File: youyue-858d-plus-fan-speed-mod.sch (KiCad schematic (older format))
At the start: 18 parts, among them P1 CONN_01X01, P2 CONN_01X01, P3 CONN_01X01, P4 CONN_01X01, U1 LM2904

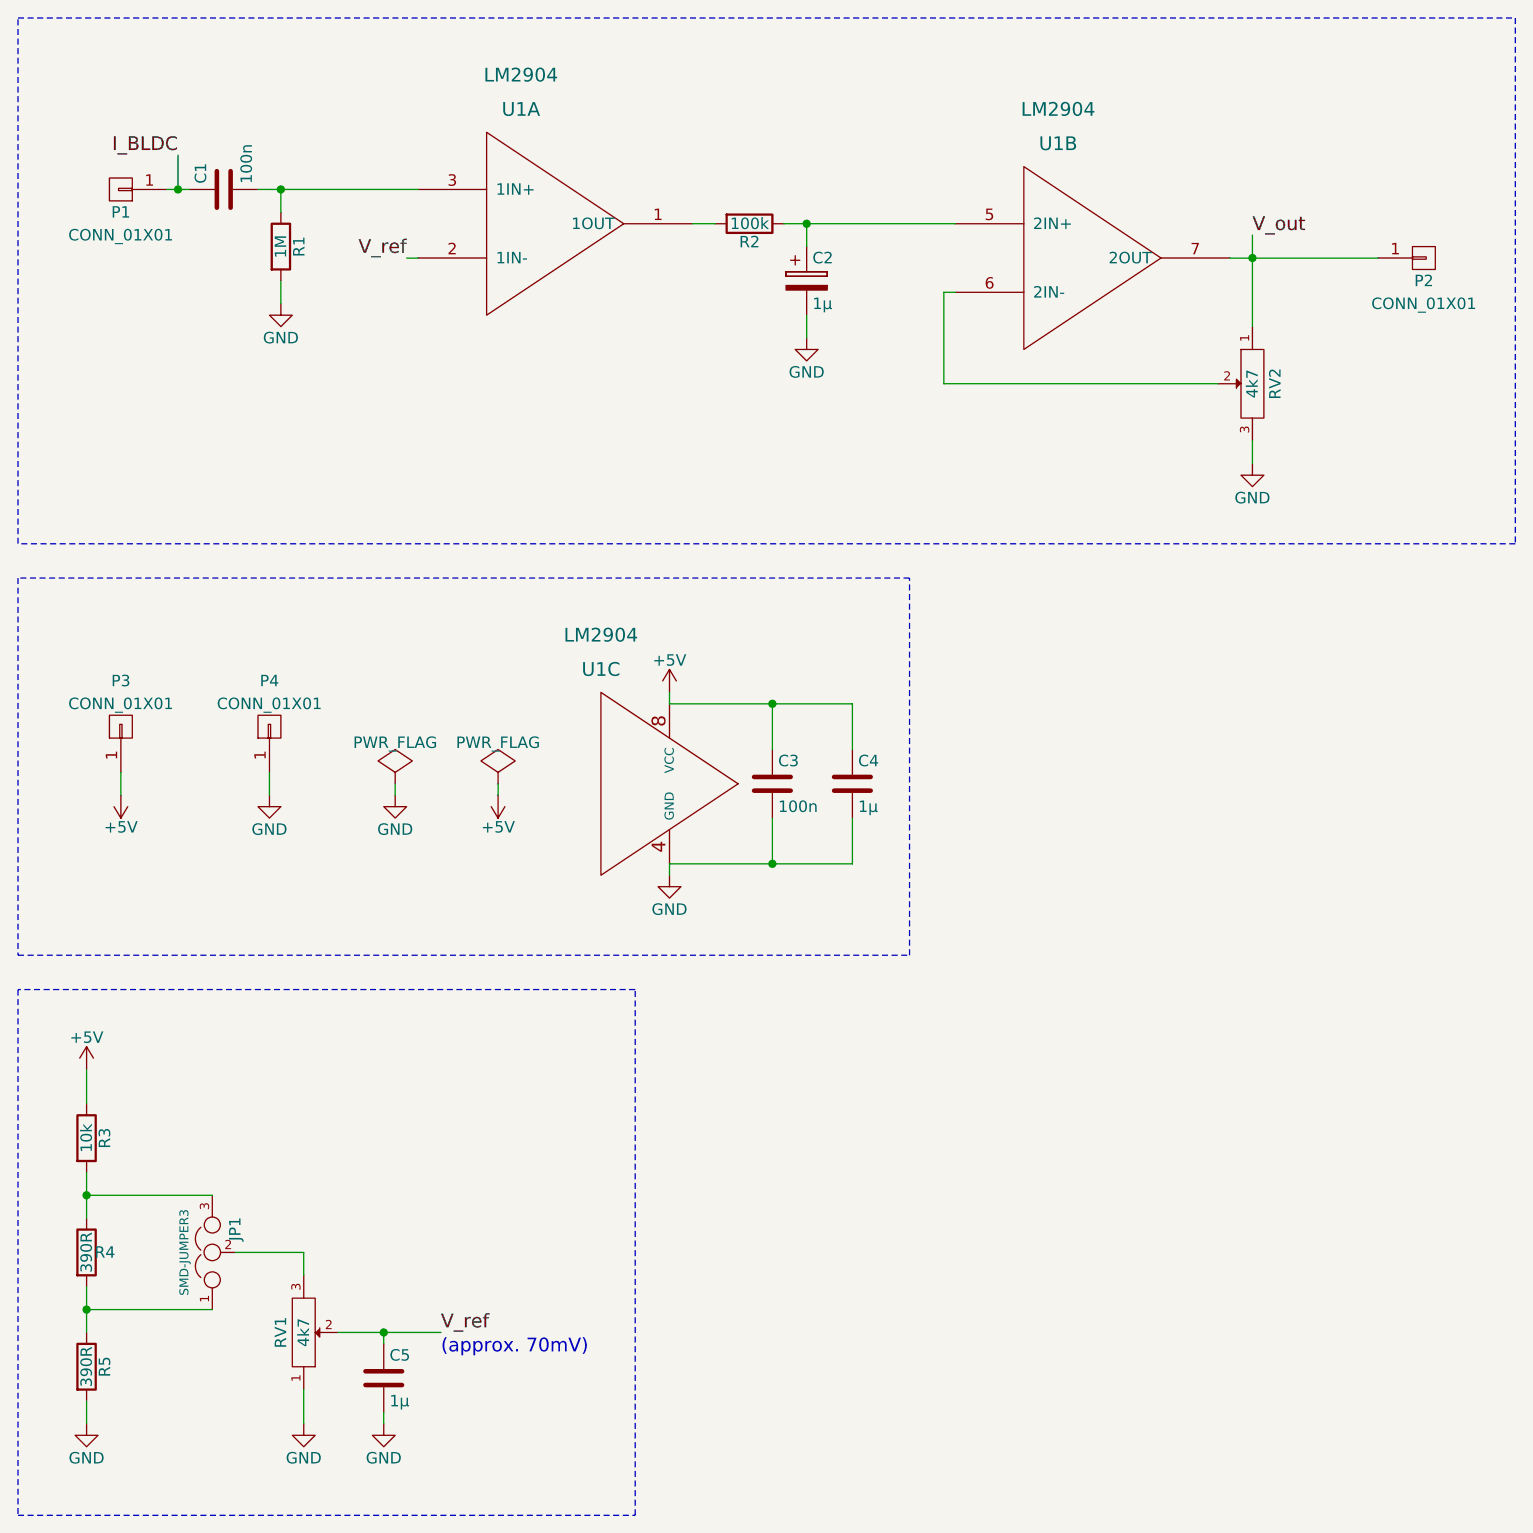
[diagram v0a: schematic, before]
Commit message: Added indicator LED for easy(er) comparator adjustment (no DSO).
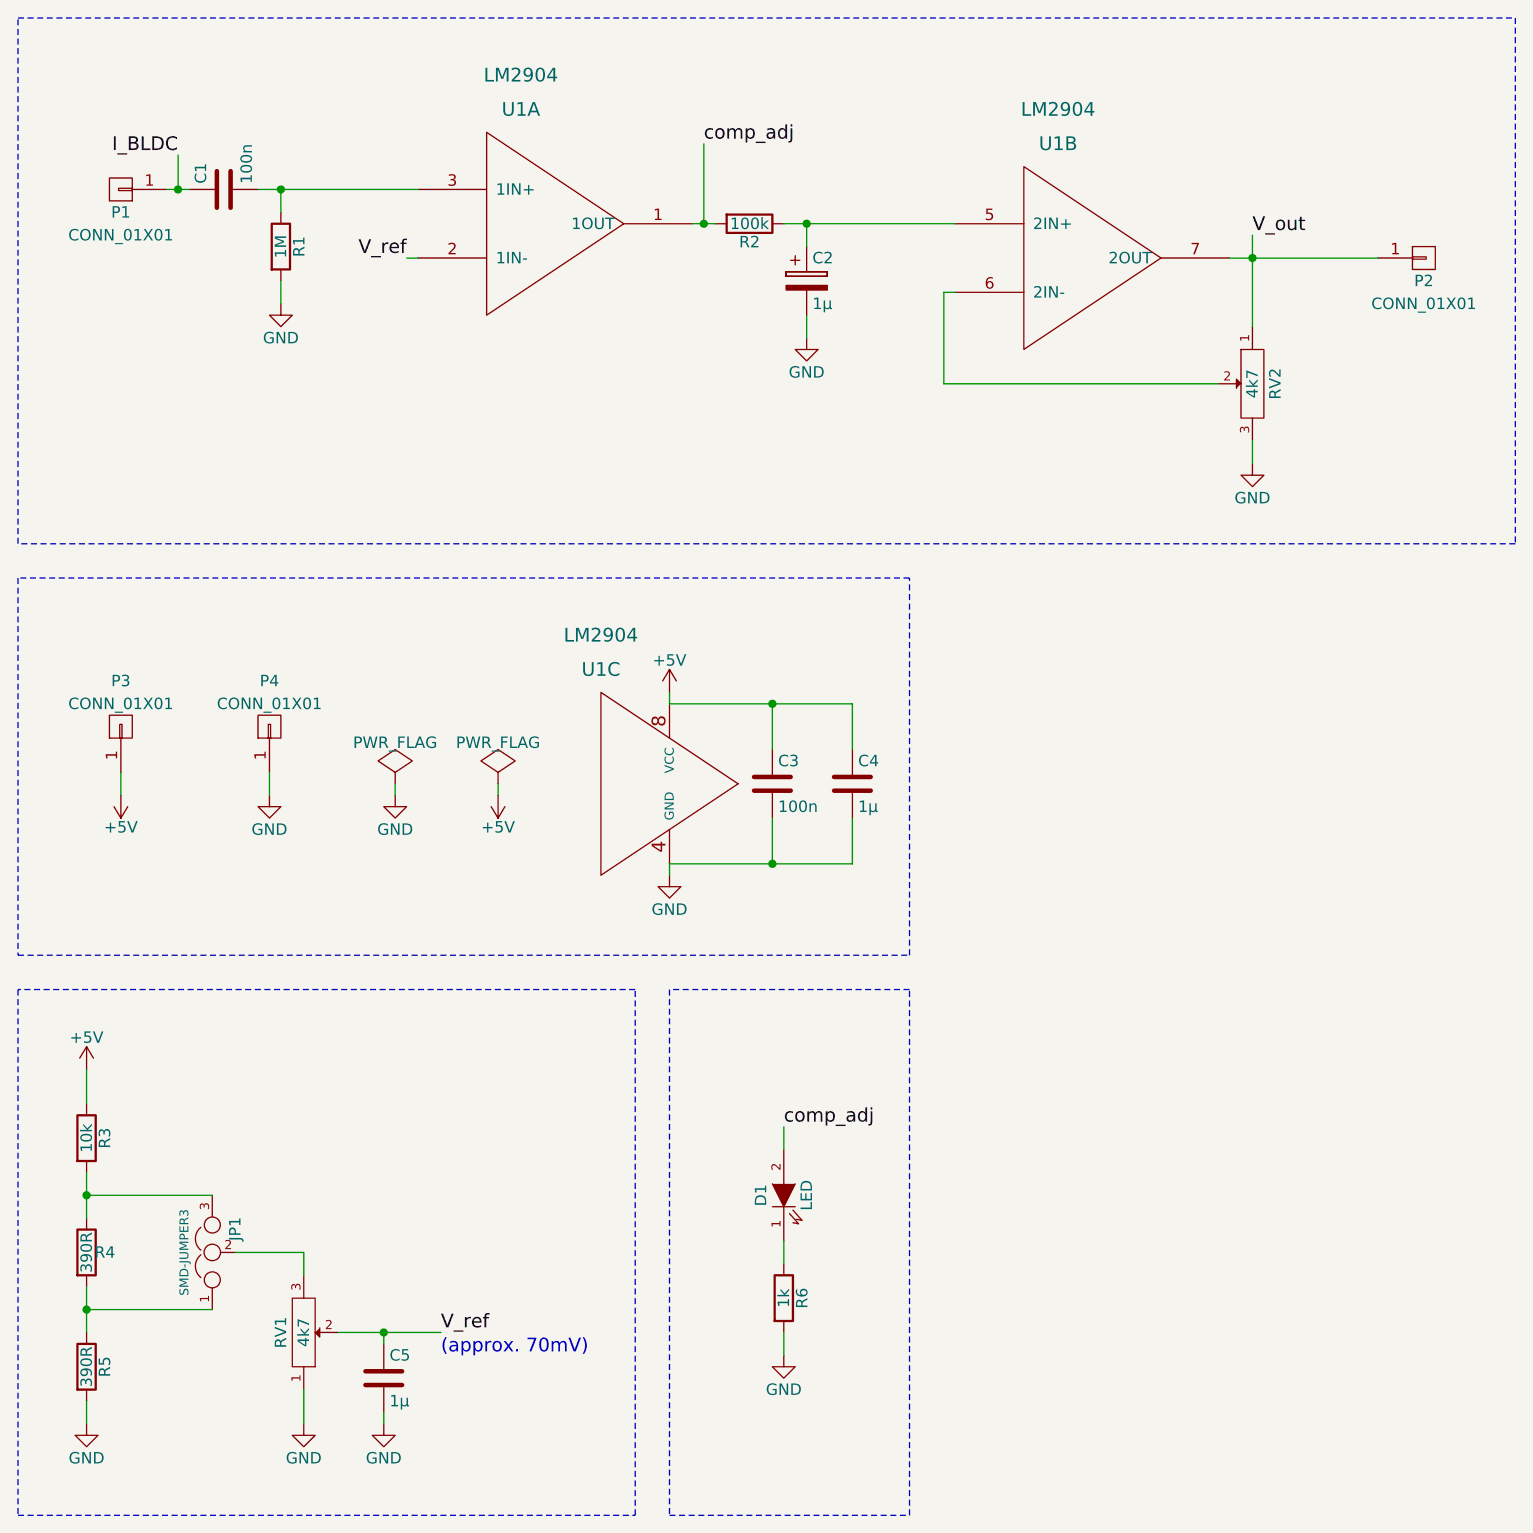
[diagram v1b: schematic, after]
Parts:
- added D1: LED, LEDs:LED-0805, symbol LED
- added R6: 1k, Resistors_SMD:R_0805_HandSoldering, symbol R
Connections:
- net GND: now also R6.2
- net comp_adj: now reaches R2.2, U1.1 (1OUT)
- net comp_adj: now also D1.2 (A)
- new net: D1.1 (K), R6.1
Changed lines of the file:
@@
 Sheet 1 1
 Title "Youyue 858D+ FAN-speed mod"
-Date "2015-10-09"
-Rev "0.10"
+Date "2015-10-24"
+Rev "0.11"
 Comp "2015 - blog.spitzenpfeil.org"
 Comment1 ""
@@
 	0    -1   -1   0
 $EndComp
-Wire Wire Line
-	3500 3600 3500 3650
-Wire Wire Line
-	3500 4350 3500 4400
-Wire Wire Line
-	3500 3650 4300 3650
-Wire Wire Line
-	3950 3650 3950 3850
-Wire Wire Line
-	3500 4350 4300 4350
-Wire Wire Line
-	3950 4350 3950 4150
-Wire Wire Line
-	4300 3650 4300 3850
-Connection ~ 3950 3650
-Wire Wire Line
-	4300 4350 4300 4150
-Connection ~ 3950 4350
-Wire Wire Line
-	950  6700 950  6800
-Wire Wire Line
-	950  6200 950  6400
-Connection ~ 950  6300
-Wire Wire Line
-	950  5800 1500 5800
-Connection ~ 950  5800
-Wire Wire Line
-	950  6300 1500 6300
 Text Label 2500 6400 0    60   ~ 0
 V_ref
-Wire Wire Line
-	1600 6050 1900 6050
 $Comp
 L GND #PWR07
@@
 	1    0    0    -1
 $EndComp
-Wire Wire Line
-	1900 6050 1900 6150
-Wire Wire Line
-	1900 6650 1900 6800
 Text Notes 2500 6500 0    60   ~ 0
 (approx. 70mV)
-Wire Wire Line
-	1700 1400 2400 1400
-Wire Wire Line
-	1800 1400 1800 1500
-Connection ~ 1800 1400
 $Comp
 L GND #PWR08
@@
 	1    0    0    -1
 $EndComp
-Wire Wire Line
-	1800 1800 1800 1900
-Wire Wire Line
-	2400 1700 2350 1700
 Text Label 2350 1700 2    60   ~ 0
 V_ref
-Wire Wire Line
-	950  5250 950  5400
-Wire Wire Line
-	950  5900 950  5700
-Wire Wire Line
-	3600 1550 3700 1550
-Wire Wire Line
-	4100 1550 4100 1650
 $Comp
 L GND #PWR09
@@
 	1    0    0    -1
 $EndComp
-Wire Wire Line
-	4100 1950 4100 2050
-Wire Wire Line
-	6050 1600 6050 2000
 $Comp
 L GND #PWR010
@@
 	1    0    0    -1
 $EndComp
-Wire Wire Line
-	6050 2500 6050 2600
-Wire Wire Line
-	4750 1850 4700 1850
-Wire Wire Line
-	4700 1850 4700 2250
-Connection ~ 4100 1550
-Wire Wire Line
-	4000 1550 4750 1550
-Wire Wire Line
-	5950 1700 6600 1700
-Wire Wire Line
-	4700 2250 5900 2250
 Text Label 1350 1250 2    60   ~ 0
 I_BLDC
 Text Label 6050 1600 0    60   ~ 0
 V_out
-Connection ~ 6050 1700
 $Comp
 L GND #PWR011
@@
 	-1   0    0    1
 $EndComp
-Wire Wire Line
-	2750 4000 2750 4050
-Wire Wire Line
-	2300 4000 2300 4050
-Wire Wire Line
-	1300 1400 1400 1400
 $Comp
 L CONN_01X01 P1
@@
 	-1   0    0    1
 $EndComp
-Wire Wire Line
-	1350 1250 1350 1400
-Connection ~ 1350 1400
 $Comp
 L CONN_01X01 P2
@@
 $EndComp
 $Comp
-L +5V #PWR015
+L +5V #PWR013
 U 1 1 56189C23
 P 1100 4050
-F 0 "#PWR015" H 1100 3900 50  0001 C CNN
+F 0 "#PWR013" H 1100 3900 50  0001 C CNN
 F 1 "+5V" H 1100 4190 50  0000 C CNN
 F 2 "" H 1100 4050 60  0000 C CNN
@@
 $EndComp
 $Comp
-L GND #PWR016
+L GND #PWR014
 U 1 1 56189C61
 P 1750 4050
-F 0 "#PWR016" H 1750 3800 50  0001 C CNN
+F 0 "#PWR014" H 1750 3800 50  0001 C CNN
 F 1 "GND" H 1750 3900 50  0000 C CNN
 F 2 "" H 1750 4050 60  0000 C CNN
@@
 	1    0    0    -1
 $EndComp
-Wire Wire Line
-	1750 3950 1750 4050
-Wire Wire Line
-	1100 3950 1100 4050
 $Comp
 L C C5
@@
 $EndComp
 $Comp
-L GND #PWR017
+L GND #PWR015
 U 1 1 5618AB05
 P 2250 6800
-F 0 "#PWR017" H 2250 6550 50  0001 C CNN
+F 0 "#PWR015" H 2250 6550 50  0001 C CNN
 F 1 "GND" H 2250 6650 50  0000 C CNN
 F 2 "" H 2250 6800 60  0000 C CNN
@@
 $EndComp
 Wire Wire Line
+	3500 3600 3500 3650
+Wire Wire Line
+	3500 4350 3500 4400
+Wire Wire Line
+	3500 3650 4300 3650
+Wire Wire Line
+	3950 3650 3950 3850
+Wire Wire Line
+	3500 4350 4300 4350
+Wire Wire Line
+	3950 4350 3950 4150
+Wire Wire Line
+	4300 3650 4300 3850
+Connection ~ 3950 3650
+Wire Wire Line
+	4300 4350 4300 4150
+Connection ~ 3950 4350
+Wire Wire Line
+	950  6700 950  6800
+Wire Wire Line
+	950  6200 950  6400
+Connection ~ 950  6300
+Wire Wire Line
+	950  5800 1500 5800
+Connection ~ 950  5800
+Wire Wire Line
+	950  6300 1500 6300
+Wire Wire Line
+	1600 6050 1900 6050
+Wire Wire Line
+	1900 6050 1900 6150
+Wire Wire Line
+	1900 6650 1900 6800
+Wire Wire Line
+	1700 1400 2400 1400
+Wire Wire Line
+	1800 1400 1800 1500
+Connection ~ 1800 1400
+Wire Wire Line
+	1800 1800 1800 1900
+Wire Wire Line
+	2400 1700 2350 1700
+Wire Wire Line
+	950  5250 950  5400
+Wire Wire Line
+	950  5900 950  5700
+Wire Wire Line
+	3600 1550 3700 1550
+Wire Wire Line
+	4100 1550 4100 1650
+Wire Wire Line
+	4100 1950 4100 2050
+Wire Wire Line
+	6050 1600 6050 2000
+Wire Wire Line
+	6050 2500 6050 2600
+Wire Wire Line
+	4750 1850 4700 1850
+Wire Wire Line
+	4700 1850 4700 2250
+Connection ~ 4100 1550
+Wire Wire Line
+	5950 1700 6600 1700
+Wire Wire Line
+	4700 2250 5900 2250
+Connection ~ 6050 1700
+Wire Wire Line
+	2750 4000 2750 4050
+Wire Wire Line
+	2300 4000 2300 4050
+Wire Wire Line
+	1300 1400 1400 1400
+Wire Wire Line
+	1350 1250 1350 1400
+Connection ~ 1350 1400
+Wire Wire Line
+	1750 3950 1750 4050
+Wire Wire Line
+	1100 3950 1100 4050
+Wire Wire Line
 	2250 6750 2250 6800
 Wire Wire Line
@@
 Wire Notes Line
 	650  2950 650  650
+Wire Wire Line
+	4000 1550 4750 1550
+Text Label 3650 1200 0    60   ~ 0
+comp_adj
+Wire Wire Line
+	3650 1200 3650 1550
+Connection ~ 3650 1550
+$Comp
+L R R6
+U 1 1 562C054C
+P 4000 6250
+F 0 "R6" V 4080 6250 50  0000 C CNN
+F 1 "1k" V 4000 6250 50  0000 C CNN
+F 2 "Resistors_SMD:R_0805_HandSoldering" V 3930 6250 30  0001 C CNN
+F 3 "" H 4000 6250 30  0000 C CNN
+	1    4000 6250
+	1    0    0    -1
+$EndComp
+$Comp
+L LED D1
+U 1 1 562C05C1
+P 4000 5800
+F 0 "D1" H 4000 5900 50  0000 C CNN
+F 1 "LED" H 4000 5700 50  0000 C CNN
+F 2 "LEDs:LED-0805" H 4000 5800 60  0001 C CNN
+F 3 "" H 4000 5800 60  0000 C CNN
+	1    4000 5800
+	0    -1   -1   0
+$EndComp
+Wire Wire Line
+	4000 6000 4000 6100
+Wire Wire Line
+	4000 6400 4000 6500
+$Comp
+L GND #PWR016
+U 1 1 562C0786
+P 4000 6500
+F 0 "#PWR016" H 4000 6250 50  0001 C CNN
+F 1 "GND" H 4000 6350 50  0000 C CNN
+F 2 "" H 4000 6500 60  0000 C CNN
+F 3 "" H 4000 6500 60  0000 C CNN
+	1    4000 6500
+	1    0    0    -1
+$EndComp
+Text Label 4000 5500 0    60   ~ 0
+comp_adj
+Wire Wire Line
+	4000 5500 4000 5600
+Wire Notes Line
+	3500 4900 3500 7200
+Wire Notes Line
+	3500 7200 4550 7200
+Wire Notes Line
+	4550 7200 4550 4900
+Wire Notes Line
+	4550 4900 3500 4900
 $EndSCHEMATC

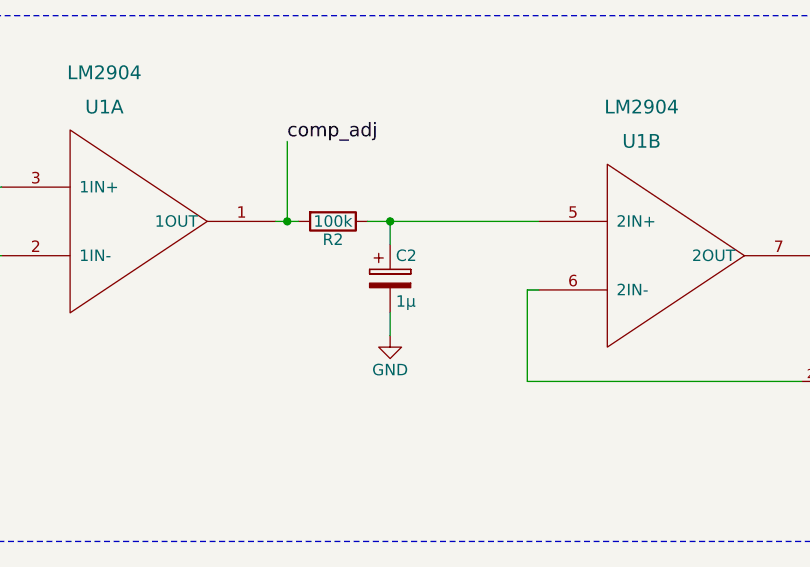
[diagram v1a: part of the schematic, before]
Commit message: Fixed 'C2' in schematic: falsely marked as electrolytic.
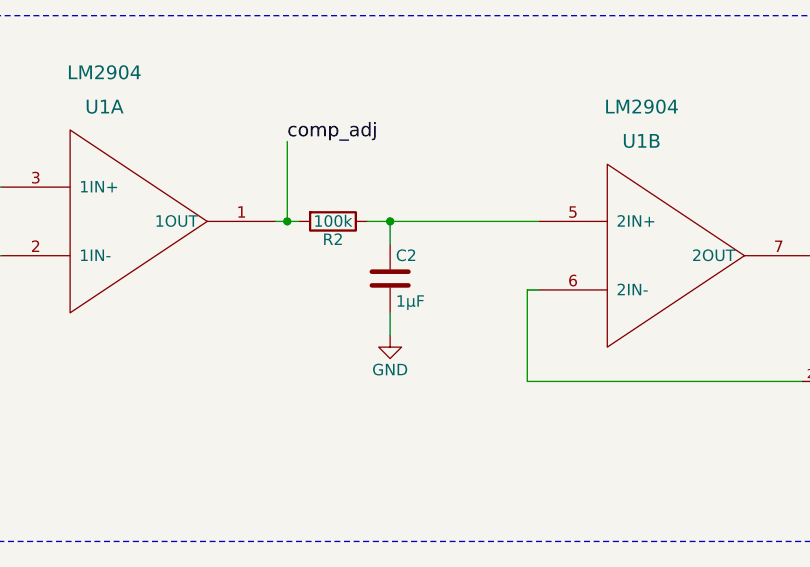
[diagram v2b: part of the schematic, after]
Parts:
- removed C2: 1µ, Capacitors_SMD:C_0805_HandSoldering, symbol CP
- added C2: 1µF, Capacitors_SMD:C_0805_HandSoldering, symbol C
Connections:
- net GND: now also C2.2
- net at R2.1, U1.5 (2IN+): now also C2.1
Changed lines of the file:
@@
 Sheet 1 1
 Title "Youyue 858D+ FAN-speed mod"
-Date "2015-10-24"
-Rev "0.11"
+Date "2015-12-03"
+Rev "0.12"
 Comp "2015 - blog.spitzenpfeil.org"
 Comment1 ""
@@
 $EndComp
 $Comp
-L CP C2
-U 1 1 5617F9EF
-P 4100 1800
-F 0 "C2" H 4125 1900 50  0000 L CNN
-F 1 "1µ" H 4125 1700 50  0000 L CNN
-F 2 "Capacitors_SMD:C_0805_HandSoldering" H 4138 1650 30  0001 C CNN
-F 3 "" H 4100 1800 60  0000 C CNN
-	1    4100 1800
-	1    0    0    -1
-$EndComp
-$Comp
 L C C1
 U 1 1 5617FA72
@@
 Wire Notes Line
 	4550 4900 3500 4900
+$Comp
+L C C2
+U 1 1 56601AF9
+P 4100 1800
+F 0 "C2" H 4125 1900 50  0000 L CNN
+F 1 "1µF" H 4125 1700 50  0000 L CNN
+F 2 "Capacitors_SMD:C_0805_HandSoldering" H 4138 1650 50  0001 C CNN
+F 3 "" H 4100 1800 50  0000 C CNN
+	1    4100 1800
+	1    0    0    -1
+$EndComp
 $EndSCHEMATC
